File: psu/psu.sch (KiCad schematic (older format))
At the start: 59 parts, among them IC101 TSR 1-24150, IC102 STM32F334K8T6, IC103 TSR 1-2450, IC104 NCP161, IC105 ADuM1201, J101 PWR_IN, J102 CTRL, J103 HV_OUT, J104 UART, P101 SWD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

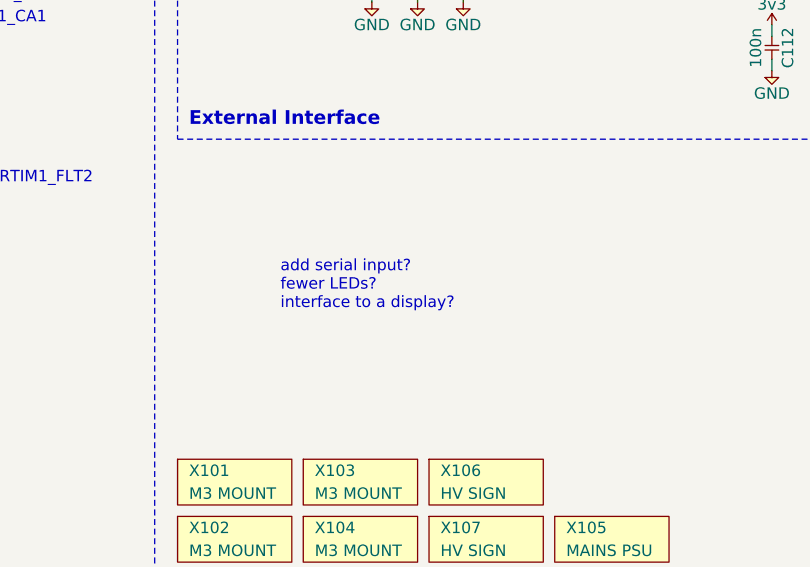
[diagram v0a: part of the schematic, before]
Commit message: Start work on driver PCB
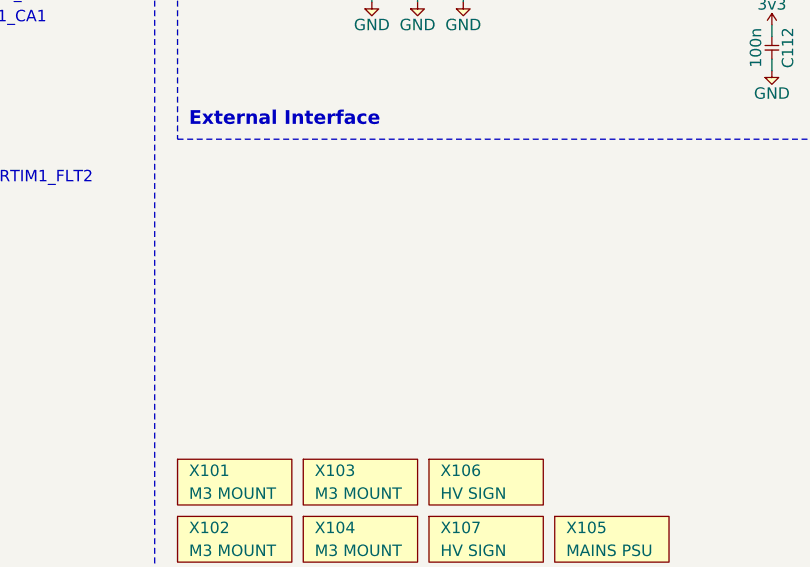
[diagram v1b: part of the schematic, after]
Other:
- note removed: "add serial input?\nfewer LEDs?\ninterface to a display?"
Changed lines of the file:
@@
 Text Label 4200 6800 0    50   ~ 0
 ~RST
-Text Notes 7450 5300 0    50   ~ 0
-add serial input?\nfewer LEDs?\ninterface to a display?
 Wire Wire Line
 	9700 1700 9800 1700
